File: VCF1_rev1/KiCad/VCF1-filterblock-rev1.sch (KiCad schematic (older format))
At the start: 28 parts, among them U1 Opamp_Dual_Generic, U2 CEM3350, U3 Opamp_Dual_Generic

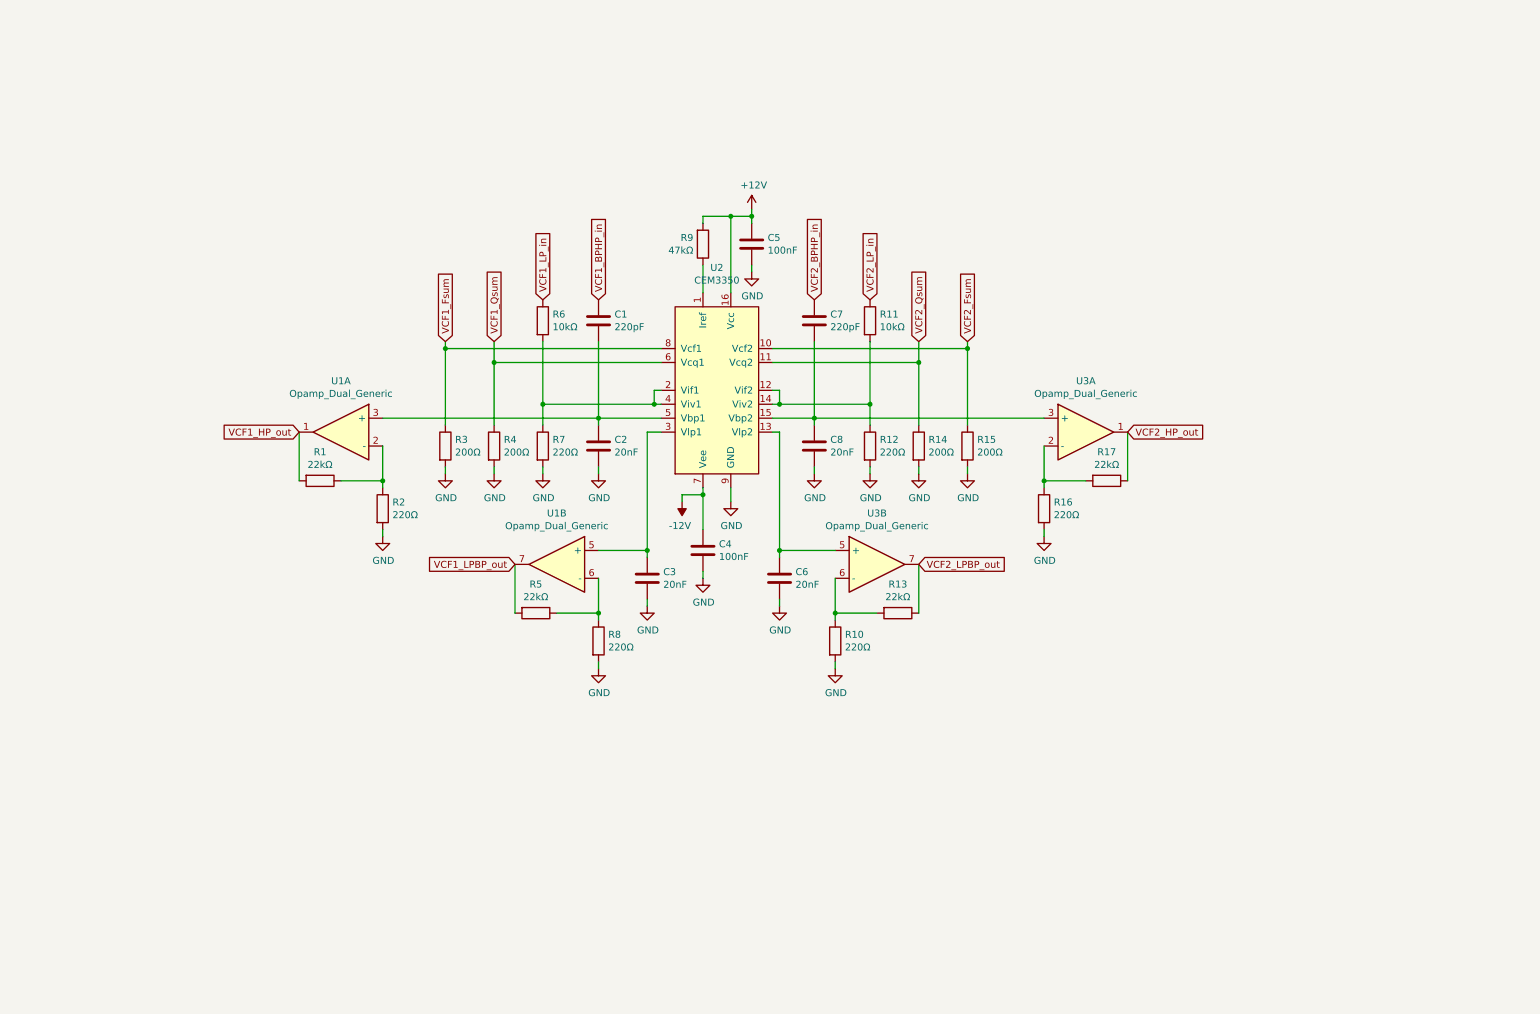
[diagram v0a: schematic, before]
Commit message: Added some initial resonance control and some other stuff.
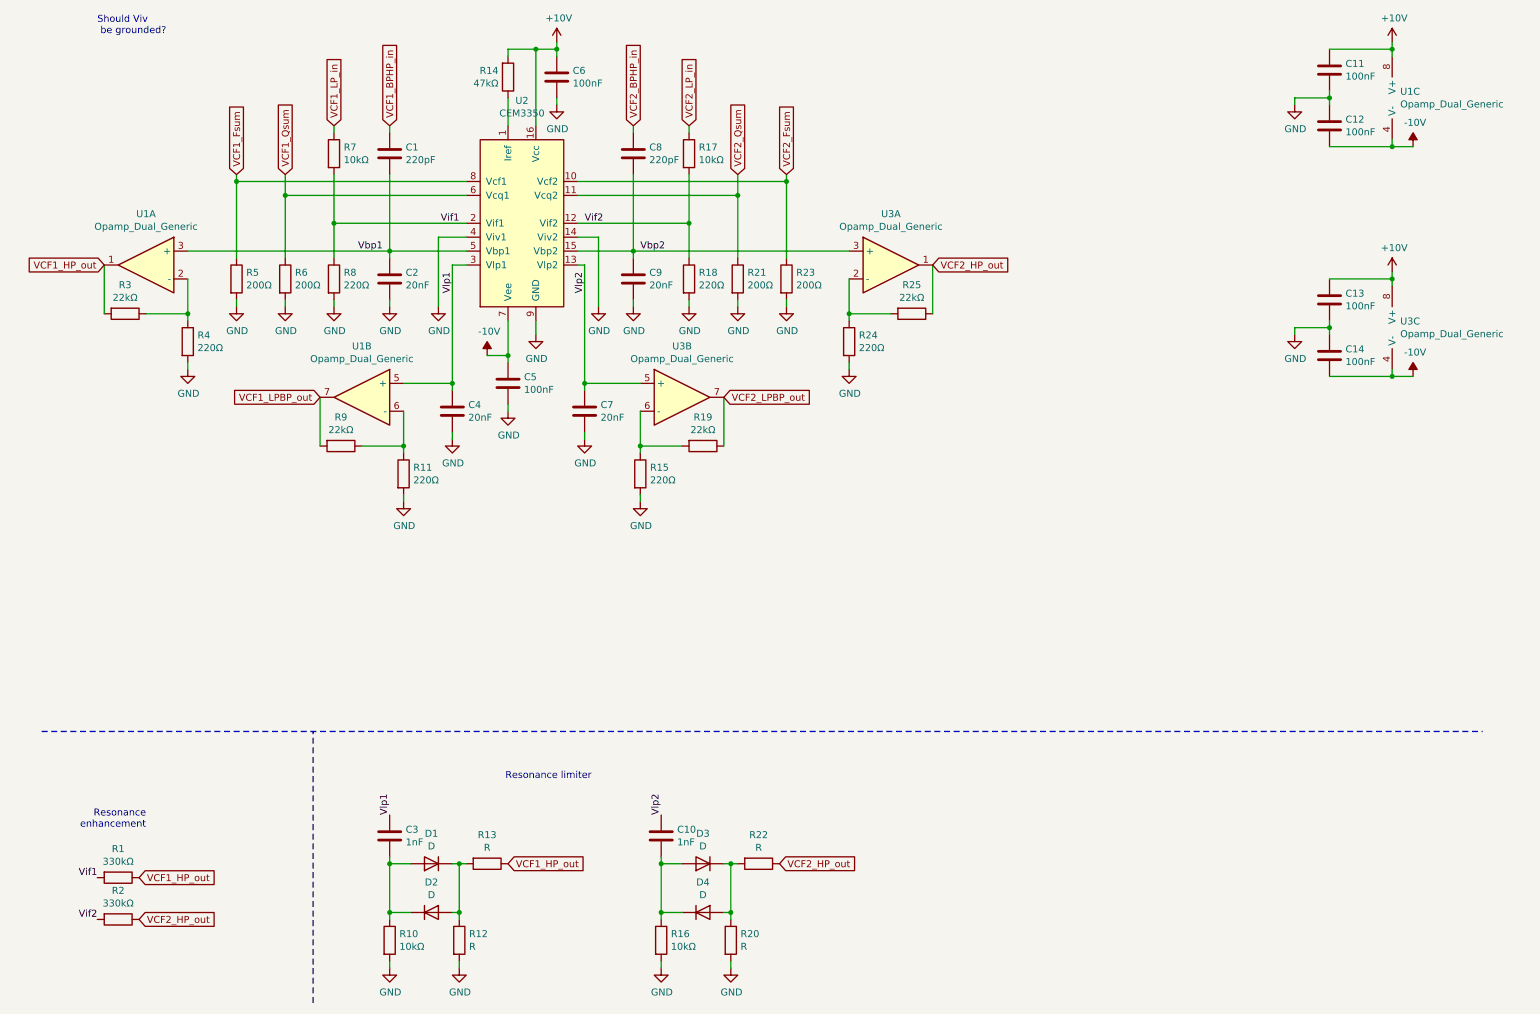
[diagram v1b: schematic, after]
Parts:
- added C10, C3: 1nF, symbol Device:C
- added C11, C12, C13, C14: 100nF, symbol Device:C
- added D1, D2, D3, D4: D, symbol Device:D
- added R1, R2: 330kΩ, symbol Device:R
- added R10, R16: 10kΩ, symbol Device:R
- added R12, R13, R20, R22: R, symbol Device:R
- added unit 3 of U1
- added unit 3 of U3
- renumbered C3 to C4, C4 to C5, C5 to C6, C6 to C7, C7 to C8, C8 to C9, R8 to R11, R9 to R14, R10 to R15, R11 to R17, R12 to R18, R13 to R19, R14 to R21, R15 to R23, R16 to R24, R17 to R25, R1 to R3, R2 to R4, R3 to R5, R4 to R6, R6 to R7, R7 to R8, R5 to R9
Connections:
- net GND: now also U2.14 (Viv2), U2.4 (Viv1), C11.2, C12.1, C13.2, C14.1, R10.2, R12.2, R16.2, R20.2
- net VCF1_HP_out: now also R1.1, R13.1
- net VCF2_HP_out: now also R2.1, R22.1
- net Vlp2: now reaches C7.1, U2.13 (Vlp2), U3.5 (+)
- net Vlp2: now also C10.1
- net Vbp1: now reaches C1.1, C2.1, U1.3 (+), U2.5 (Vbp1)
- net Vlp1: now reaches C4.1, U1.5 (+), U2.3 (Vlp1)
- net Vlp1: now also C3.1
- net Vbp2: now reaches C8.1, C9.1, U2.15 (Vbp2), U3.3 (+)
- net Vif2: now reaches R17.2, R18.1, U2.12 (Vif2)
- net Vif2: now also R2.2; no longer U2.14 (Viv2)
- net Vif1: now reaches R7.2, R8.1, U2.2 (Vif1)
- net Vif1: now also R1.2; no longer U2.4 (Viv1)
- net +12V renamed +10V
- net +10V: now also C11.1, C13.1, U1.8 (V+), U3.8 (V+)
- net -12V renamed -10V
- net -10V: now also C12.2, C14.2, U1.4 (V-), U3.4 (V-)
- new net: D1.1 (K), D2.2 (A), R12.1, R13.2
- new net: C3.2, D1.2 (A), D2.1 (K), R10.1
- new net: D3.1 (K), D4.2 (A), R20.1, R22.2
- new net: C10.2, D3.2 (A), D4.1 (K), R16.1
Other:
- note added: "Resonance limiter"
- note added: "Resonance\nenhancement"
- note added: "Should Viv\n be grounded?"
- moved on the sheet: C1, C2, C4, C5, C6, C7, C8, C9, R11, R14, R15, R17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
